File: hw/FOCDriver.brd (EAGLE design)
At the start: 99.1 x 62.2 mm, 118 parts, among them Q1 BC817, Q2 BC817, Q3 BC817, Q4 BC817, Q5 BC817, Q6 BC817, U1 SN74LVC2G17, U10 LMV321SQ3T2G, U11 LMV321SQ3T2G, U2 AO4606, U3 BA7805FP, U4 SN74LVC2G17, U5 AO4606, U6 SN74LVC2G17, U7 AO4606, U8 LMV321SQ3T2G, U9 LMV321SQ3T2G

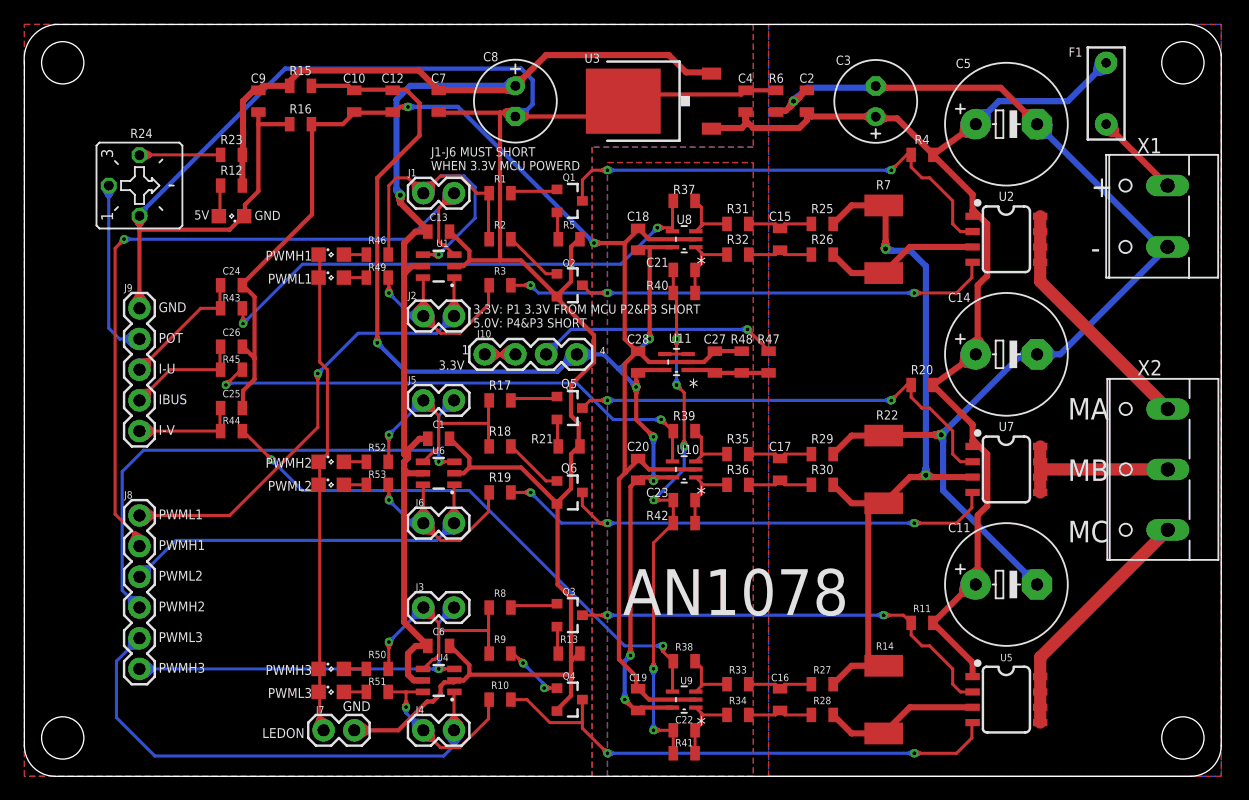
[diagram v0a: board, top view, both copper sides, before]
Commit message: refine top silk
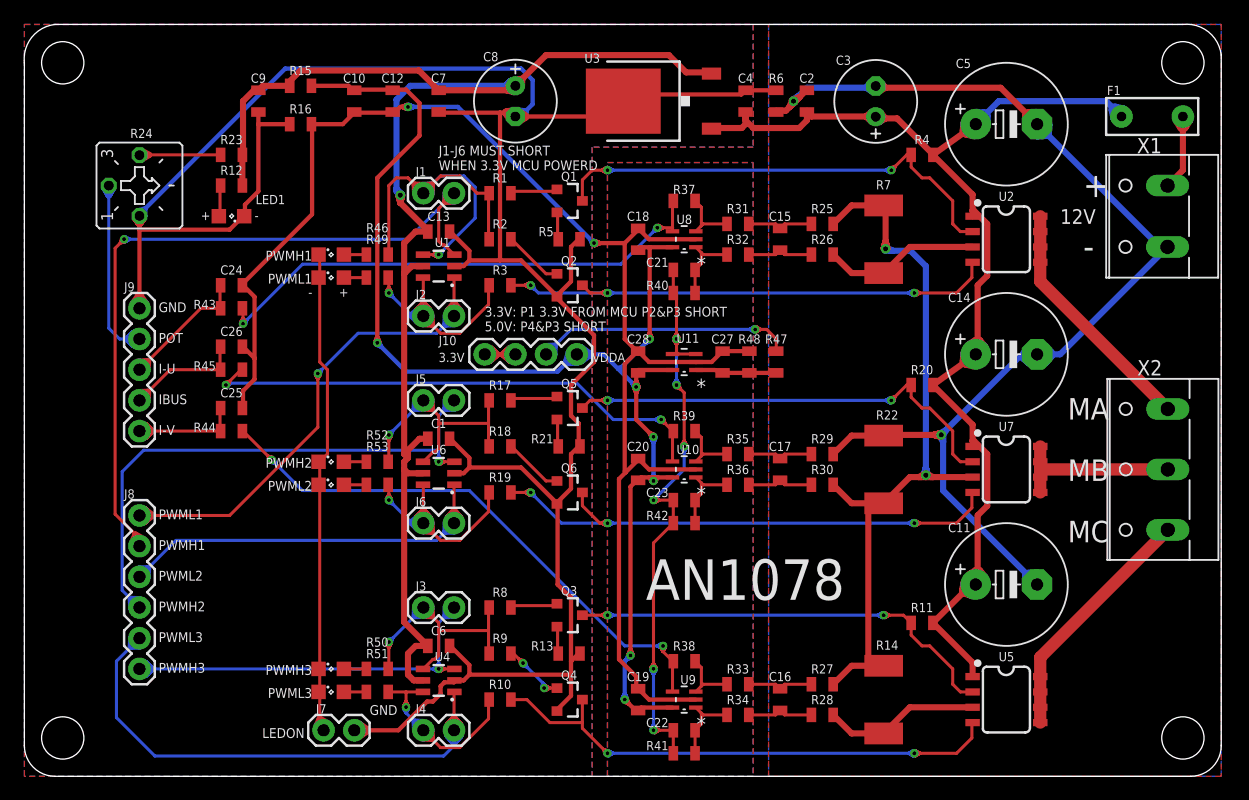
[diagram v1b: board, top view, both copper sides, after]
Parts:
- moved F1 4.26 mm to (93.3, 54.6), turned to 180 degrees
- moved C27 0.63 mm to (57.8, 34.3)
- moved R47 0.63 mm to (62.2, 34.3)
- moved R48 0.63 mm to (60.0, 34.3)
- moved U11 0.63 mm to (54.6, 34.3)
- renumbered 5V to LED1
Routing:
- net VREF: track 158.5 -> 176.5 mm
- net VDDA: track 191.6 -> 206.3 mm
- net N$3: track 103.0 -> 115.1 mm
- net N$9: track 100.8 -> 112.9 mm
- net N$8: track 74.1 -> 80.5 mm
- net N$6: track 67.7 -> 73.7 mm
- net N$10: track 69.5 -> 75.5 mm
- net N$21: track 69.0 -> 74.7 mm
- net AGND: track 150.0 -> 155.3 mm
- net L2: track 69.7 -> 74.8 mm
- net H2: track 79.3 -> 83.7 mm
- net L2O: track 39.9 -> 43.9 mm
- net N$7: track 75.1 -> 78.7 mm
- net PWRDIV: track 34.2 -> 30.8 mm
- net N$26: track 59.1 -> 62.0 mm
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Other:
- board text added: "12V"
- board text added: "VDDA"
- board text removed: "1"
- board text removed: "4"

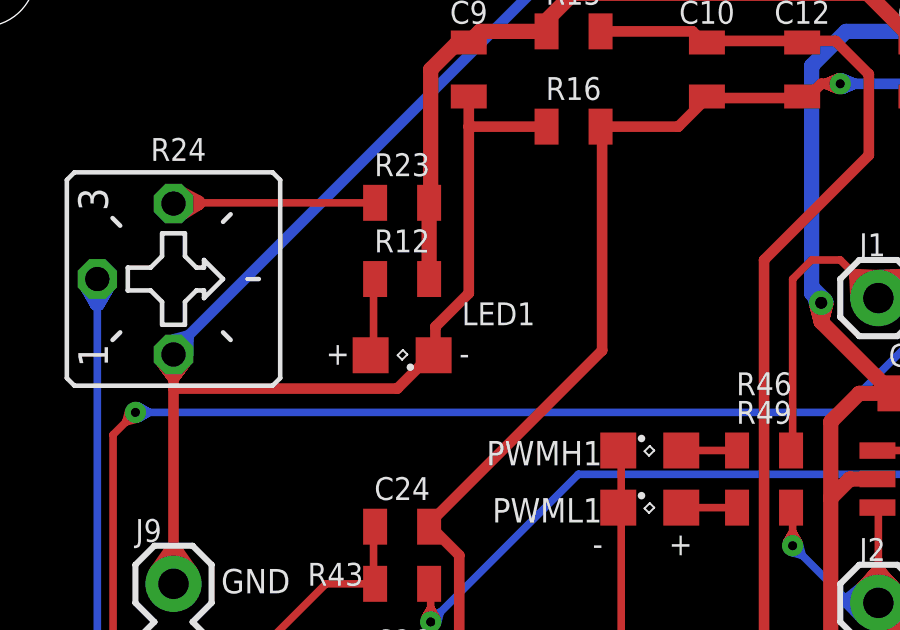
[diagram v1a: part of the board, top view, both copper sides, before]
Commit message: refine top silk
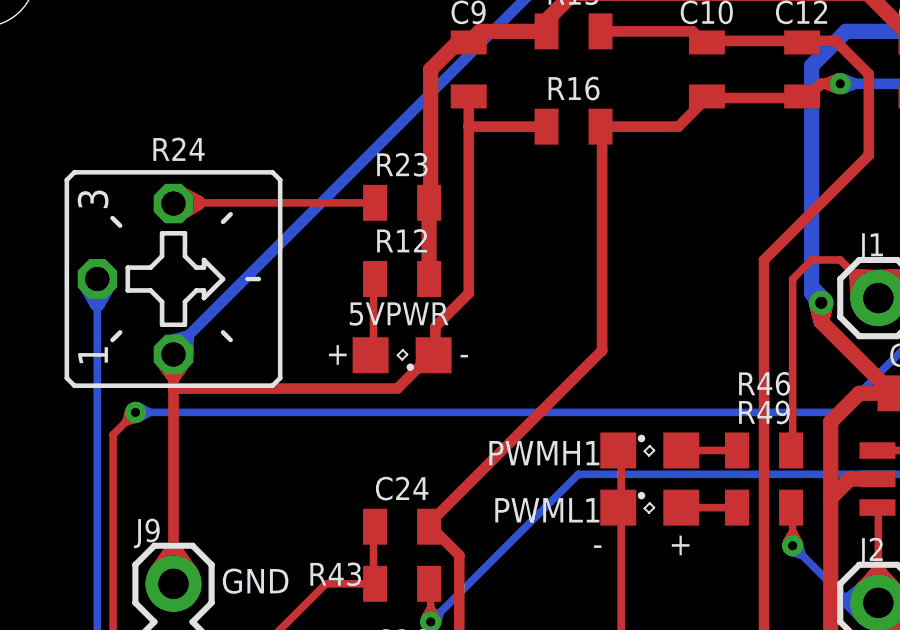
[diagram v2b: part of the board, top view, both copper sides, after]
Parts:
- renumbered LED1 to 5VPWR
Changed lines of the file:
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@@
 </autorouter>
 <elements>
-<element name="LED1" library="led" package="SML0805" value="ORANGE" x="17.145" y="46.355" smashed="yes" rot="R180">
-<attribute name="NAME" x="19.1375" y="47.355" size="0.762" layer="25" ratio="12"/>
+<element name="5VPWR" library="led" package="SML0805" value="ORANGE" x="17.145" y="46.355" smashed="yes" rot="R180">
+<attribute name="NAME" x="15.3275" y="47.355" size="0.762" layer="25" ratio="12"/>
 <attribute name="VALUE" x="18.645" y="48.355" size="1.27" layer="27" rot="R180"/>
 </element>
@@
 <contactref element="C13" pad="2"/>
 <contactref element="R24" pad="A"/>
-<contactref element="LED1" pad="C"/>
+<contactref element="5VPWR" pad="C"/>
 <contactref element="C8" pad="-"/>
 <contactref element="C7" pad="2"/>
@@
 </signal>
 <signal name="N$31">
-<contactref element="LED1" pad="A"/>
+<contactref element="5VPWR" pad="A"/>
 <contactref element="R12" pad="1"/>
 <wire x1="16.1925" y1="48.895" x2="16.1925" y2="46.355" width="0.254" layer="1"/>

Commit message: fix error
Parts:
- removed C28: 0.1uF, SparkFun-Capacitors:0805
- added C29: 0.1u, rcl:C0805
- added J11: (no value), SparkFun-Connectors:1X02
- C1, C10, C12, C13, C6, C7, C9: value 0.1uF -> 100n; device SparkFun-Capacitors:0805 -> rcl:C0805
- C15, C16, C17, C21, C22, C23: value 56pF -> 56p; device SparkFun-Capacitors:0805 -> rcl:C0805
- C18, C19, C2, C20, C27, C4: value 0.1uF -> 0.1u; device SparkFun-Capacitors:0805 -> rcl:C0805
- C24, C25, C26: value 1nF -> 1n; device SparkFun-Capacitors:0805 -> rcl:C0805
- Q1, Q2, Q3, Q4, Q5, Q6: device SparkFun-DiscreteSemi:SOT23-3 -> transistor-npn:SOT23-BEC
- R1, R10, R11, R12, R13, R17, R18, R19, R2, R20, R21, R23, R3, R4, R46, R49, R5, R50, R51, R52, R53, R8, R9: device SparkFun-Resistors:0805 -> rcl:R0805
- R15: value 1R -> 0; device SparkFun-Resistors:0805 -> rcl:R0805
- R16, R6: value 0R -> 0; device SparkFun-Resistors:0805 -> rcl:R0805
- R25, R26, R27, R28, R29, R30, R31, R32, R33, R34, R35, R36, R43, R44, R45: value 1K 1% -> 1K; device SparkFun-Resistors:0805 -> rcl:R0805
- R37, R38, R39, R40, R41, R42, R47, R48: value 20K 1% -> 20K; device SparkFun-Resistors:0805 -> rcl:R0805
- moved F1 20.4 mm to (73.0, 56.5), turned to 270 degrees
- moved J2 17.5 mm to (22.9, 50.2), turned to 0 degrees
- moved J4 17.1 mm to (22.9, 15.2), turned to 0 degrees
- moved J5 16.7 mm to (22.9, 20.3), turned to 0 degrees
- moved J6 16.3 mm to (22.9, 31.1), turned to 0 degrees
- moved J3 15.9 mm to (22.9, 4.45), turned to 0 degrees
- moved J1 15.5 mm to (22.9, 39.4), turned to 0 degrees
- moved LED3 11.3 mm to (34.3, 48.3), turned to 180 degrees
- moved C1 11.1 mm to (24.1, 23.5)
- moved LED5 10.9 mm to (34.3, 13.3), turned to 180 degrees
- moved U1 10.9 mm to (24.1, 46.0), turned to 90 degrees
- moved C6 10.6 mm to (24.1, 7.62)
- moved U4 10.6 mm to (24.1, 11.1), turned to 90 degrees
- moved C13 10.5 mm to (24.1, 42.5)
- moved U6 10.3 mm to (24.1, 27.0), turned to 90 degrees
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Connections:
- net 5V: now also C1.2, C13.2, C6.2, J11.2, R23.1; no longer C1.1, C13.1, C6.1, R23.2
- net AGND: now also C29.2; no longer C28.2
- net DGND: now also C1.1, C13.1, C6.1, J11.1, Q2.E, Q4.E, Q6.E; no longer C1.2, C13.2, C6.2, Q2.2, Q4.2, Q6.2
- net ICOM: now also U7.1; no longer U7.3
- net IU: now also U2.1; no longer U2.3
- net IV: now also U5.1; no longer U5.3
- net N$10: now also Q1.C, U2.4; no longer Q1.3, U2.2
- net N$15: now also C21.1; no longer C21.2
- net N$20: now also C22.1; no longer C22.2
- net N$25: now also C23.1; no longer C23.2
- net N$28: now also Q5.E; no longer Q5.2
- net N$3: now also Q6.C, U7.2; no longer Q6.3, U7.4
- net N$30: now also Q1.B; no longer Q1.1
- net N$32: now also Q2.B; no longer Q2.1
- net N$39: now also Q3.B; no longer Q3.1
- net N$4: now also R23.2; no longer R23.1
- net N$40: now also Q1.E; no longer Q1.2
- net N$41: now also Q4.B; no longer Q4.1
- net N$42: now also Q5.B; no longer Q5.1
- net N$43: now also Q3.E; no longer Q3.2
- net N$44: now also Q6.B; no longer Q6.1
- net N$6: now also Q5.C, U7.4; no longer Q5.3, U7.2
- net N$7: now also Q4.C, U5.2; no longer Q4.3, U5.4
- net N$8: now also Q3.C, U5.4; no longer Q3.3, U5.2
- net N$9: now also Q2.C, U2.2; no longer Q2.3, U2.4
- net VDDA: now also C29.1; no longer C28.1
- net VIN: now also U2.3, U5.3, U7.3; no longer U2.1, U5.1, U7.1
- net VREF: now also C21.2, C22.2, C23.2; no longer C21.1, C22.1, C23.1
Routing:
- net DGND: track 234.5 -> 351.6 mm, vias 0 -> 8
- net VREF: track 176.5 -> 78.2 mm, vias 6 -> 4
- net VDDA: track 206.3 -> 136.6 mm, vias 7 -> 5
- net N$9: track 112.9 -> 51.0 mm, vias 3 -> 2
- net LEDON: track 43.5 -> 104.6 mm, vias 0 -> 5
- net N$3: track 115.1 -> 64.6 mm, vias 3 -> 2
- net AGND: track 155.3 -> 200.6 mm, vias 2 -> 6
- net L2: track 74.8 -> 31.0 mm
- net N$8: track 80.5 -> 37.2 mm, vias 2 -> 0
- net H2: track 83.7 -> 42.0 mm, vias 1 -> 0
- net H1: track 79.5 -> 40.2 mm, vias 1 -> 0
- net N$10: track 75.5 -> 37.2 mm, vias 2 -> 0
- net H3: track 72.8 -> 34.7 mm, vias 1 -> 0
- net N$6: track 73.7 -> 36.3 mm, vias 2 -> 0
- net N$7: track 78.7 -> 45.0 mm, vias 2 -> 0
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- removed copper zone on layer 1, net AGND
- removed copper zone on layer 16, net AGND
- removed copper zone on layer 1, net DGND
- removed copper zone on layer 16, net DGND
- removed copper zone on layer 1, net GND
- removed copper zone on layer 16, net GND
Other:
- board size 99.1 x 62.2 mm -> 99.1 x 62.3 mm
